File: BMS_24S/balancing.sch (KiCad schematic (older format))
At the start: 0 parts

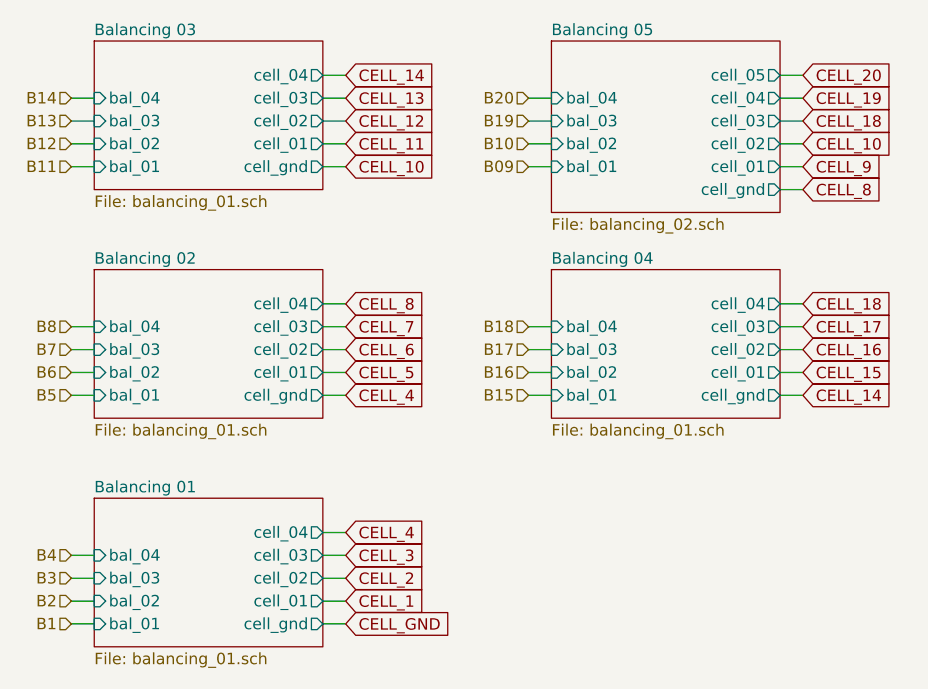
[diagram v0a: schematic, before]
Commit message: update balancing circuit
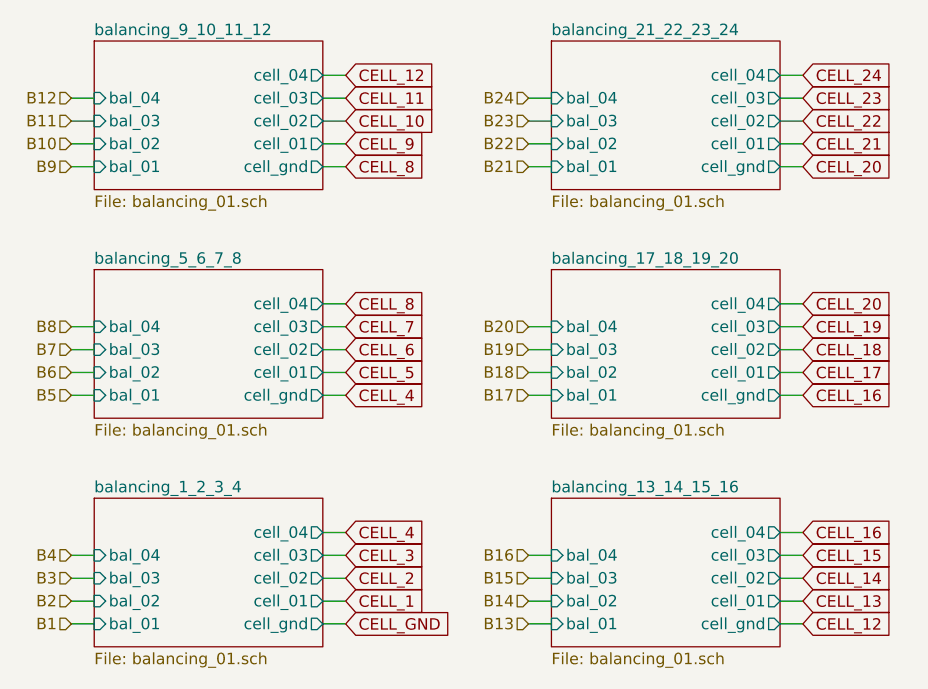
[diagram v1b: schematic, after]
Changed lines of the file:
@@
 $Descr User 8268 5827
 encoding utf-8
-Sheet 26 32
+Sheet 24 31
 Title ""
 Date ""
@@
 S 4000 3000 1000 650
 U 5F255A50
-F0 "Balancing 01" 50
+F0 "balancing_1_2_3_4" 50
 F1 "balancing_01.sch" 50
 F2 "cell_02" O R 5000 3350 50
@@
 	3900 3250 4000 3250
 Text GLabel 5100 1450 2    50   Input ~ 0
-CELL_11
+CELL_9
 Text GLabel 5100 3450 2    50   Input ~ 0
 CELL_1
@@
 CELL_2
 Text GLabel 5100 1550 2    50   Input ~ 0
-CELL_10
+CELL_8
 Text GLabel 5100 3250 2    50   Input ~ 0
 CELL_3
-Text GLabel 7100 1550 2    50   Input ~ 0
-CELL_9
 Text GLabel 5100 3150 2    50   Input ~ 0
 CELL_4
@@
 Text GLabel 5100 2350 2    50   Input ~ 0
 CELL_6
-Text GLabel 7100 1150 2    50   Input ~ 0
-CELL_20
-Text GLabel 7100 1250 2    50   Input ~ 0
-CELL_19
-Text GLabel 7100 2150 2    50   Input ~ 0
-CELL_18
-Text GLabel 7100 2250 2    50   Input ~ 0
-CELL_17
-Text GLabel 7100 2350 2    50   Input ~ 0
+Text GLabel 7100 3150 2    50   Input ~ 0
 CELL_16
-Text GLabel 7100 2450 2    50   Input ~ 0
+Text GLabel 7100 3250 2    50   Input ~ 0
 CELL_15
+Text GLabel 7100 3350 2    50   Input ~ 0
+CELL_14
+Text GLabel 7100 3450 2    50   Input ~ 0
+CELL_13
 Text GLabel 5100 1150 2    50   Input ~ 0
-CELL_14
+CELL_12
 Text GLabel 5100 1250 2    50   Input ~ 0
-CELL_13
+CELL_11
 Text GLabel 5100 3550 2    50   Input ~ 0
 CELL_GND
@@
 S 4000 2000 1000 650
 U 5F34C39A
-F0 "Balancing 02" 50
+F0 "balancing_5_6_7_8" 50
 F1 "balancing_01.sch" 50
 F2 "cell_02" O R 5000 2350 50
@@
 S 4000 1000 1000 650
 U 5F34DE6D
-F0 "Balancing 03" 50
+F0 "balancing_9_10_11_12" 50
 F1 "balancing_01.sch" 50
 F2 "cell_02" O R 5000 1350 50
@@
 F10 "bal_01" I L 4000 1550 50
 $EndSheet
-Text HLabel 5900 1550 0    50   Input ~ 0
-B09
-Text HLabel 5900 1450 0    50   Input ~ 0
+Text HLabel 3900 1550 0    50   Input ~ 0
+B9
+Text HLabel 3900 1450 0    50   Input ~ 0
 B10
-Text HLabel 3900 1550 0    50   Input ~ 0
+Wire Wire Line
+	3900 1550 4000 1550
+Wire Wire Line
+	3900 1450 4000 1450
+Wire Wire Line
+	3900 1350 4000 1350
+Wire Wire Line
+	3900 1250 4000 1250
+Wire Wire Line
+	5000 1550 5100 1550
+Wire Wire Line
+	5000 1450 5100 1450
+Wire Wire Line
+	5000 1350 5100 1350
+Wire Wire Line
+	5000 1250 5100 1250
+Wire Wire Line
+	5000 1150 5100 1150
+$Sheet
+S 6000 3000 1000 650
+U 5F352741
+F0 "balancing_13_14_15_16" 50
+F1 "balancing_01.sch" 50
+F2 "cell_02" O R 7000 3350 50
+F3 "cell_01" O R 7000 3450 50
+F4 "cell_03" O R 7000 3250 50
+F5 "cell_04" O R 7000 3150 50
+F6 "cell_gnd" O R 7000 3550 50
+F7 "bal_02" I L 6000 3450 50
+F8 "bal_03" I L 6000 3350 50
+F9 "bal_04" I L 6000 3250 50
+F10 "bal_01" I L 6000 3550 50
+$EndSheet
+Text HLabel 3900 1350 0    50   Input ~ 0
 B11
-Text HLabel 3900 1450 0    50   Input ~ 0
+Text HLabel 3900 1250 0    50   Input ~ 0
 B12
-Wire Wire Line
-	3900 1550 4000 1550
-Wire Wire Line
-	3900 1450 4000 1450
-Wire Wire Line
-	3900 1350 4000 1350
-Wire Wire Line
-	3900 1250 4000 1250
-Wire Wire Line
-	5000 1550 5100 1550
-Wire Wire Line
-	5000 1450 5100 1450
-Wire Wire Line
-	5000 1350 5100 1350
-Wire Wire Line
-	5000 1250 5100 1250
-Wire Wire Line
-	5000 1150 5100 1150
+Text HLabel 5900 3550 0    50   Input ~ 0
+B13
+Text HLabel 5900 3450 0    50   Input ~ 0
+B14
+Wire Wire Line
+	5900 3550 6000 3550
+Wire Wire Line
+	5900 3450 6000 3450
+Wire Wire Line
+	5900 3350 6000 3350
+Wire Wire Line
+	5900 3250 6000 3250
+Wire Wire Line
+	7000 3550 7100 3550
+Wire Wire Line
+	7000 3450 7100 3450
+Wire Wire Line
+	7000 3350 7100 3350
+Wire Wire Line
+	7000 3250 7100 3250
+Wire Wire Line
+	7000 3150 7100 3150
+Text HLabel 5900 3350 0    50   Input ~ 0
+B15
+Text HLabel 5900 3250 0    50   Input ~ 0
+B16
+Text GLabel 5100 2550 2    50   Input ~ 0
+CELL_4
+Text GLabel 5100 1350 2    50   Input ~ 0
+CELL_10
+Text GLabel 7100 3550 2    50   Input ~ 0
+CELL_12
+Text GLabel 7100 2150 2    50   Input ~ 0
+CELL_20
+Text GLabel 7100 2250 2    50   Input ~ 0
+CELL_19
+Text GLabel 7100 2350 2    50   Input ~ 0
+CELL_18
+Text GLabel 7100 2450 2    50   Input ~ 0
+CELL_17
 $Sheet
 S 6000 2000 1000 650
-U 5F352741
-F0 "Balancing 04" 50
+U 5F7CE31F
+F0 "balancing_17_18_19_20" 50
 F1 "balancing_01.sch" 50
 F2 "cell_02" O R 7000 2350 50
@@
 F10 "bal_01" I L 6000 2550 50
 $EndSheet
-Text HLabel 3900 1350 0    50   Input ~ 0
-B13
-Text HLabel 3900 1250 0    50   Input ~ 0
-B14
 Text HLabel 5900 2550 0    50   Input ~ 0
-B15
+B17
 Text HLabel 5900 2450 0    50   Input ~ 0
-B16
+B18
 Wire Wire Line
 	5900 2550 6000 2550
@@
 	7000 2150 7100 2150
 Text HLabel 5900 2350 0    50   Input ~ 0
-B17
+B19
 Text HLabel 5900 2250 0    50   Input ~ 0
-B18
-Text HLabel 5900 1350 0    50   Input ~ 0
-B19
-Text HLabel 5900 1250 0    50   Input ~ 0
 B20
-Wire Wire Line
-	5900 1550 6000 1550
-Wire Wire Line
-	5900 1450 6000 1450
-Wire Wire Line
-	5900 1350 6000 1350
-Wire Wire Line
-	5900 1250 6000 1250
-Wire Wire Line
-	7000 1650 7100 1650
-Wire Wire Line
-	7000 1550 7100 1550
-Wire Wire Line
-	7000 1450 7100 1450
-Wire Wire Line
-	7000 1350 7100 1350
-Wire Wire Line
-	7000 1250 7100 1250
-Text GLabel 5100 2550 2    50   Input ~ 0
-CELL_4
-Text GLabel 7100 1650 2    50   Input ~ 0
-CELL_8
-Text GLabel 5100 1350 2    50   Input ~ 0
-CELL_12
 Text GLabel 7100 2550 2    50   Input ~ 0
-CELL_14
-$Sheet
-S 6000 1000 1000 750
-U 5F355BC0
-F0 "Balancing 05" 50
-F1 "balancing_02.sch" 50
-F2 "cell_02" O R 7000 1450 50
-F3 "cell_01" O R 7000 1550 50
-F4 "cell_03" O R 7000 1350 50
-F5 "cell_04" O R 7000 1250 50
-F6 "cell_gnd" O R 7000 1650 50
+CELL_16
+Text GLabel 7100 1150 2    50   Input ~ 0
+CELL_24
+Text GLabel 7100 1250 2    50   Input ~ 0
+CELL_23
+Text GLabel 7100 1350 2    50   Input ~ 0
+CELL_22
+Text GLabel 7100 1450 2    50   Input ~ 0
+CELL_21
+$Sheet
+S 6000 1000 1000 650
+U 5F7CF78E
+F0 "balancing_21_22_23_24" 50
+F1 "balancing_01.sch" 50
+F2 "cell_02" O R 7000 1350 50
+F3 "cell_01" O R 7000 1450 50
+F4 "cell_03" O R 7000 1250 50
+F5 "cell_04" O R 7000 1150 50
+F6 "cell_gnd" O R 7000 1550 50
 F7 "bal_02" I L 6000 1450 50
 F8 "bal_03" I L 6000 1350 50
 F9 "bal_04" I L 6000 1250 50
 F10 "bal_01" I L 6000 1550 50
-F11 "cell_05" O R 7000 1150 50
-$EndSheet
-Text GLabel 7100 1450 2    50   Input ~ 0
-CELL_10
-Text GLabel 7100 1350 2    50   Input ~ 0
-CELL_18
-Wire Wire Line
-	7100 1150 7000 1150
+$EndSheet
+Text HLabel 5900 1550 0    50   Input ~ 0
+B21
+Text HLabel 5900 1450 0    50   Input ~ 0
+B22
+Wire Wire Line
+	5900 1550 6000 1550
+Wire Wire Line
+	5900 1450 6000 1450
+Wire Wire Line
+	5900 1350 6000 1350
+Wire Wire Line
+	5900 1250 6000 1250
+Wire Wire Line
+	7000 1550 7100 1550
+Wire Wire Line
+	7000 1450 7100 1450
+Wire Wire Line
+	7000 1350 7100 1350
+Wire Wire Line
+	7000 1250 7100 1250
+Wire Wire Line
+	7000 1150 7100 1150
+Text HLabel 5900 1350 0    50   Input ~ 0
+B23
+Text HLabel 5900 1250 0    50   Input ~ 0
+B24
+Text GLabel 7100 1550 2    50   Input ~ 0
+CELL_20
 $EndSCHEMATC
